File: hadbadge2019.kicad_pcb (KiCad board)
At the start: 4 copper layers, 88 x 140.5 mm, 194 parts, among them J1 Conn_02x05_Odd_Even, J10 Conn_01x02_Male, J11 NO STUFF, J12 NO STUFF, J2 USB_B_Micro, J3 NO STUFF, J4 HDMI_A_1.4, J5 FH26W-45S-0.3SHW(60), J6 Conn_02x20_Odd_Even, J7 Conn_02x03_Odd_Even, J8 Conn_02x03_Odd_Even, J9 Conn_01x02_Male, Q1 AO3400, Q2 AO3401, Q3 AO3400, Q4 AO3400, Q5 AO3400, SW1 Up, SW2 Down, SW3 Left, SW4 Right, SW5 A, SW6 B, SW7 Select, SW8 Start, SW9 SW_SPDT_shielded, U1 LFE5Ux-45F, U10 NS8002, U11 74LVC1G175, U12 RPM973, U2 LY68L6400SLIT, U3 LY68L6400SLIT, U4 W25Q128JVSIQ, U5 M3406, U6 XC6206P25, U7 XR1151, U8 74LVC1G3157, U9 XR1151, X1 X1G004481001400

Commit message: Starting to add fixes for final ver
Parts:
- added H1: MountingHole, MountingHole:MountingHole_3.5mm, B.Cu at (100.1, 111.4)
- added R72: 1K, Resistor_SMD:R_0603_1608Metric, B.Cu at (132.3, 141.5)
- R57: value 100 -> 1K
- moved R7 24.2 mm to (97.3, 101.5), turned to 270 degrees
- moved U8 7.42 mm to (100.1, 105.1)
- moved R56 3.78 mm to (105.2, 106.2), turned to 270 degrees
- moved C12 1.02 mm to (96.9, 126.2), turned to 0 degrees
- turned R69 to 0 degrees
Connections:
- D10 pad 2: CATR -> CATC
- D10 pad 3: CATG -> CATB
- D10 pad 4: CATB -> CATA
- D11 pad 2: CATR -> CATC
- D11 pad 3: CATG -> CATB
- D11 pad 4: CATB -> CATA
- D12 pad 2: CATR -> CATB
- D12 pad 3: CATG -> CATA
- D12 pad 4: CATB -> CATC
- D13 pad 2: CATR -> CATB
- D13 pad 3: CATG -> CATA
- D13 pad 4: CATB -> CATC
- D14 pad 2: CATR -> CATA
- D14 pad 3: CATG -> CATB
- D14 pad 4: CATB -> CATC
- D15 pad 2: CATR -> CATA
- D15 pad 3: CATG -> CATB
- D15 pad 4: CATB -> CATC
- D5 pad 2: CATR -> CATA
- D5 pad 3: CATG -> CATB
- D5 pad 4: CATB -> CATC
- D6 pad 2: CATR -> CATC
- D6 pad 3: CATG -> CATB
- D6 pad 4: CATB -> CATA
- D7 pad 2: CATR -> CATA
- D7 pad 3: CATG -> CATB
- D7 pad 4: CATB -> CATC
- D8 pad 2: CATR -> CATC
- D8 pad 3: CATG -> CATB
- D8 pad 4: CATB -> CATA
- D9 pad 2: CATR -> CATA
- D9 pad 3: CATG -> CATB
- D9 pad 4: CATB -> CATC
- J1 pad 4: (no net) -> Net-(J1-Pad4)
- Q3 pad 3: CATR -> CATA
- Q4 pad 3: CATG -> CATB
- Q5 pad 3: CATB -> CATC
- R69 pad 1: LEDR -> VIO
- R69 pad 2: GND -> LEDR
- SW9 pad 3: (no net) -> Net-(SW9-Pad3)
- U1 pad C13: (no net) -> Net-(U1-PadC13)
- U1 pad D12: (no net) -> Net-(U1-PadD12)
- U1 pad D13: (no net) -> Net-(U1-PadD13)
- U1 pad D14: (no net) -> Net-(U1-PadD14)
- U1 pad D15: (no net) -> Net-(U1-PadD15)
- U1 pad D7: (no net) -> Net-(U1-PadD7)
- U1 pad D8: (no net) -> Net-(U1-PadD8)
- U1 pad E10: (no net) -> Net-(U1-PadE10)
- U1 pad E11: (no net) -> Net-(U1-PadE11)
- U1 pad E12: (no net) -> Net-(U1-PadE12)
- U1 pad E13: (no net) -> Net-(U1-PadE13)
- U1 pad E14: (no net) -> Net-(U1-PadE14)
- U1 pad E15: (no net) -> Net-(U1-PadE15)
- U1 pad E16: (no net) -> GENIO_29
- U1 pad E18: (no net) -> Net-(U1-PadE18)
- U1 pad E6: (no net) -> Net-(U1-PadE6)
- U1 pad E7: (no net) -> Net-(U1-PadE7)
- U1 pad E8: (no net) -> Net-(U1-PadE8)
- U1 pad E9: (no net) -> Net-(U1-PadE9)
- U1 pad F16: (no net) -> Net-(U1-PadF16)
- U1 pad F18: (no net) -> GENIO_25
- U1 pad F5: (no net) -> Net-(U1-PadF5)
- U1 pad G16: (no net) -> Net-(U1-PadG16)
- U1 pad G5: (no net) -> Net-(U1-PadG5)
- U1 pad H16: (no net) -> GENIO_26
- U1 pad H3: (no net) -> Net-(U1-PadH3)
- U1 pad H4: (no net) -> Net-(U1-PadH4)
- U1 pad H5: (no net) -> Net-(U1-PadH5)
- U1 pad J17: (no net) -> Net-(U1-PadJ17)
- U1 pad J18: (no net) -> Net-(U1-PadJ18)
- U1 pad J5: (no net) -> Net-(U1-PadJ5)
- U1 pad K16: (no net) -> Net-(U1-PadK16)
- U1 pad K17: (no net) -> Net-(U1-PadK17)
- U1 pad K5: (no net) -> Net-(U1-PadK5)
- U1 pad L19: (no net) -> Net-(U1-PadL19)
- U1 pad L5: (no net) -> Net-(U1-PadL5)
- U1 pad M17: (no net) -> Net-(U1-PadM17)
- U1 pad M18: (no net) -> Net-(U1-PadM18)
- U1 pad M19: (no net) -> Net-(U1-PadM19)
- U1 pad M5: (no net) -> Net-(U1-PadM5)
- U1 pad N16: (no net) -> Net-(U1-PadN16)
- U1 pad N17: (no net) -> Net-(U1-PadN17)
- U1 pad N18: (no net) -> Net-(U1-PadN18)
- U1 pad N5: (no net) -> Net-(U1-PadN5)
- U1 pad P16: (no net) -> Net-(U1-PadP16)
- U1 pad P17: (no net) -> Net-(U1-PadP17)
- U1 pad P18: (no net) -> Net-(U1-PadP18)
- U1 pad R17: (no net) -> Net-(U1-PadR17)
- U1 pad R3: (no net) -> Net-(U1-PadR3)
- U1 pad T17: (no net) -> Net-(U1-PadT17)
- U1 pad T2: (no net) -> Net-(U1-PadT2)
- U1 pad T20: (no net) -> Net-(U1-PadT20)
- U1 pad T3: (no net) -> Net-(U1-PadT3)
- U1 pad V1: (no net) -> Net-(U1-PadV1)
- U1 pad W10: (no net) -> Net-(U1-PadW10)
- U1 pad W11: (no net) -> Net-(U1-PadW11)
- U1 pad W13: (no net) -> Net-(U1-PadW13)
- U1 pad W14: (no net) -> Net-(U1-PadW14)
- U1 pad W17: (no net) -> Net-(U1-PadW17)
- U1 pad W18: (no net) -> Net-(U1-PadW18)
- U1 pad W20: (no net) -> Net-(U1-PadW20)
- U1 pad W4: (no net) -> Net-(U1-PadW4)
- U1 pad W5: (no net) -> Net-(U1-PadW5)
- U1 pad W8: (no net) -> Net-(U1-PadW8)
- U1 pad W9: (no net) -> Net-(U1-PadW9)
- U1 pad Y11: (no net) -> Net-(U1-PadY11)
- U1 pad Y12: (no net) -> Net-(U1-PadY12)
- U1 pad Y14: (no net) -> Net-(U1-PadY14)
- U1 pad Y15: (no net) -> Net-(U1-PadY15)
- U1 pad Y16: (no net) -> Net-(U1-PadY16)
- U1 pad Y17: (no net) -> Net-(U1-PadY17)
- U1 pad Y19: (no net) -> Net-(U1-PadY19)
- U1 pad Y5: (no net) -> Net-(U1-PadY5)
- U1 pad Y6: (no net) -> Net-(U1-PadY6)
- U1 pad Y7: (no net) -> Net-(U1-PadY7)
- U1 pad Y8: (no net) -> Net-(U1-PadY8)
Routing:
- net CATA: track 0.00 -> 191.5 mm, vias 0 -> 12
- net CATC: track 0.00 -> 186.8 mm, vias 0 -> 6
- net CATR: track 182.4 -> 0.00 mm, vias 6 -> 0
- net CATG: track 180.4 -> 0.00 mm, vias 16 -> 0
- net VIO: track 95.7 -> 106.2 mm, vias 21 -> 23
- net Net-(U11-Pad4): track 7.86 -> 15.8 mm
- net CATB: track 191.9 -> 185.6 mm, vias 4 -> 15
- net LED11: track 19.0 -> 24.6 mm, vias 1 -> 2
- net BTN_UP: track 33.9 -> 39.1 mm
- net GND: track 327.9 -> 322.8 mm
- net /FPGA/FLASH_CS_INT: track 42.1 -> 37.2 mm, vias 4 -> 3
- net ADCREF: track 24.7 -> 26.1 mm
- net LED6: track 97.6 -> 99.0 mm
- net LED4: track 99.8 -> 101.2 mm
- net LED5: track 98.5 -> 99.8 mm
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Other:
- board text added: "2019, SPRITE_TM SPRITESMODS.COM"
- board text added: "GPIO3 DRM"
- board text added: "Hackaday Supercon 2019 Badge Final Version All the bugs on this badge not caught in the prototypes are now official features."
- board text added: "J11: PMOD PMODB4 PMODA4 PMODB3 PMODA3 PMODB2 PMODA2 PMODB1 PMODA1 GND GND 3V3 3V3"
- board text added: "J1: RX TX TCK TMS TDO TDI KEY 3V3 GND VBAT"
- board text added: "J3 (OTHER SIDE): INSERT SPEAKER HERE."
- board text added: "J8 & J11: SAO V1.69 BIS X-TREME! HDRS"
- board text added: "VIO GND SCL SDA GPIO2 GPIO1"
- board text removed: "DRM GPIO3"
- board text removed: "Hackaday Supercon 2019 Badge Proto v3 If you have this, you are hyper-l33t, and/or get to suffer through the last few bugs that the final version won't have."
- board text removed: "J11: PMOD 3V3 3V3 GND GND PMODA1 PMODB1 PMODA2 PMODB2 PMODA3 PMODB3 PMODA4 PMODB4"
- board text removed: "J1: VBAT GND 3V3 KEY TDI TDO TMS TCK TX RX"
- board text removed: "J8-J11: SAO V1.69 BIS X-TREME! HDRS GPIO1 GPIO2 SDA SCL GND 3V3"

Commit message: Final version
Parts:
- added REF**: mouse_bite_6, lib:mouse_bite_6, F.Cu at (143.3, 25.2)
- added REF**: mouse_bite_6, lib:mouse_bite_6, F.Cu at (113.7, 25.2)
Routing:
- net VBAT: track 306.6 -> 302.4 mm
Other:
- outline, holes or cut-outs redrawn
- board text added: "BAT NEG"
- board text added: "BAT POS"
- board text added: "REMOVE ME"

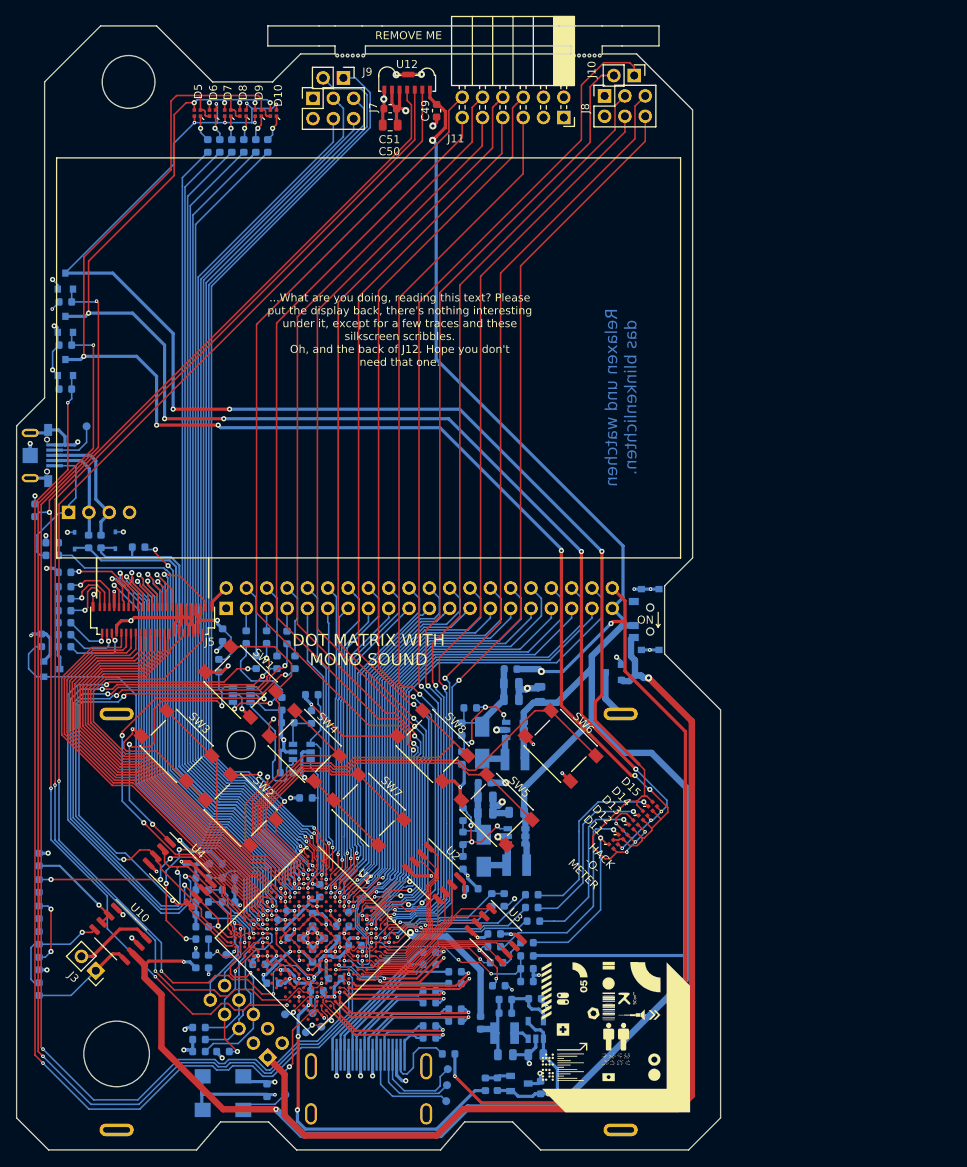
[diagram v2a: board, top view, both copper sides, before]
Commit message: Final changes: add some fiducials, clean up vias. Ready for prod, I hope.
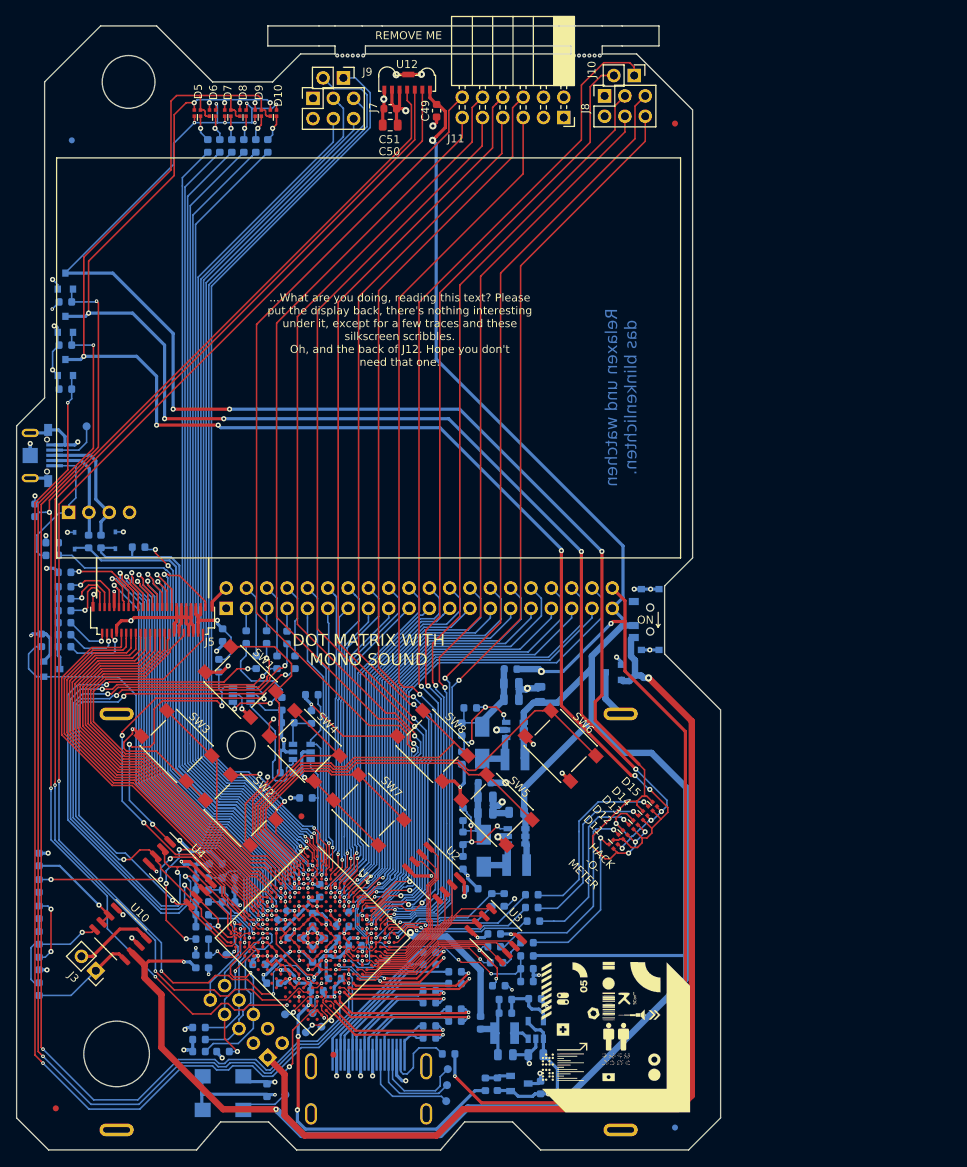
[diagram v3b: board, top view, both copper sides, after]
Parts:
- added FID1: Fiducial, Fiducial:Fiducial_0.75mm_Mask1.5mm, F.Cu at (107.6, 120.3)
- added FID2: Fiducial, Fiducial:Fiducial_0.75mm_Mask1.5mm, F.Cu at (111.6, 150.1)
- added FID3: Fiducial, Fiducial:Fiducial_0.75mm_Mask1.5mm, F.Cu at (76.9, 156.8)
- added FID4: Fiducial, Fiducial:Fiducial_0.75mm_Mask1.5mm, F.Cu at (154.3, 33.7)
- added FID5: Fiducial, Fiducial:Fiducial_0.75mm_Mask1.5mm, B.Cu at (154.3, 159.2)
- added FID6: Fiducial, Fiducial:Fiducial_0.75mm_Mask1.5mm, B.Cu at (78.9, 35.8)
- SW1: value Up -> Up (RED)
- SW2: value Down -> Down (RED)
- SW3: value Left -> Left (RED)
- SW4: value Right -> Right (RED)
- SW5: value A -> A (RED)
- SW6: value B -> B (RED)
- SW7: value Select -> Select (BLUE)
- SW8: value Start -> Start (BLUE)
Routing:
- net CATC: track 186.8 -> 187.3 mm

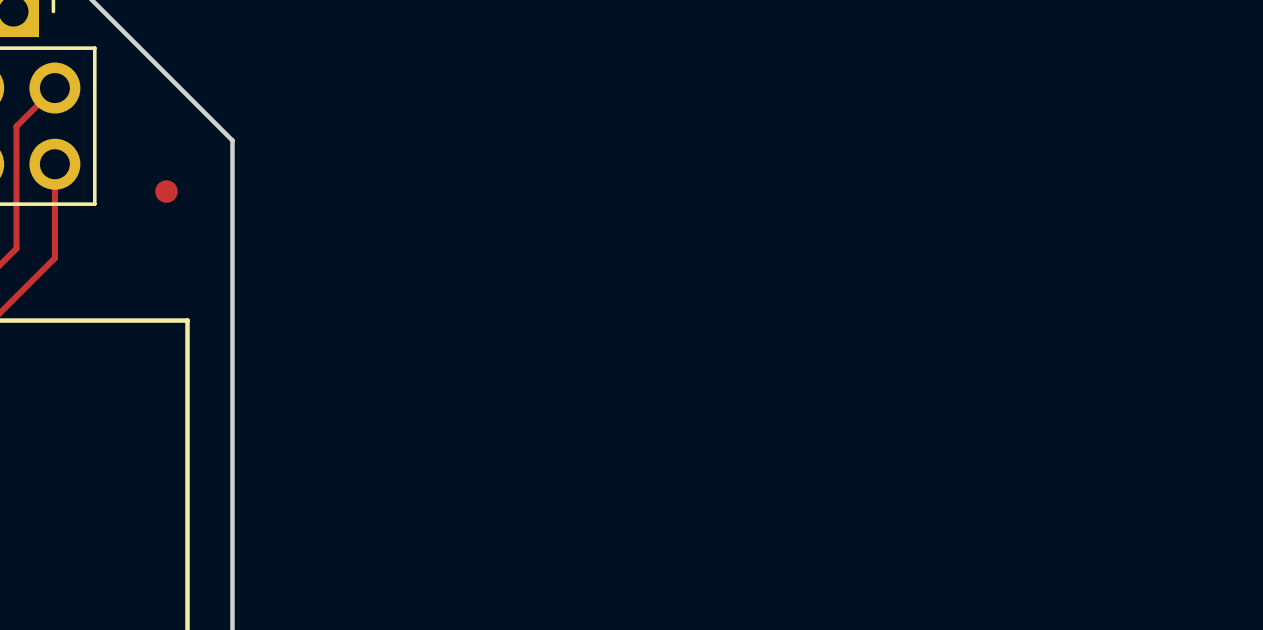
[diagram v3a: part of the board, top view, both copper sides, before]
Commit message: Add known issues
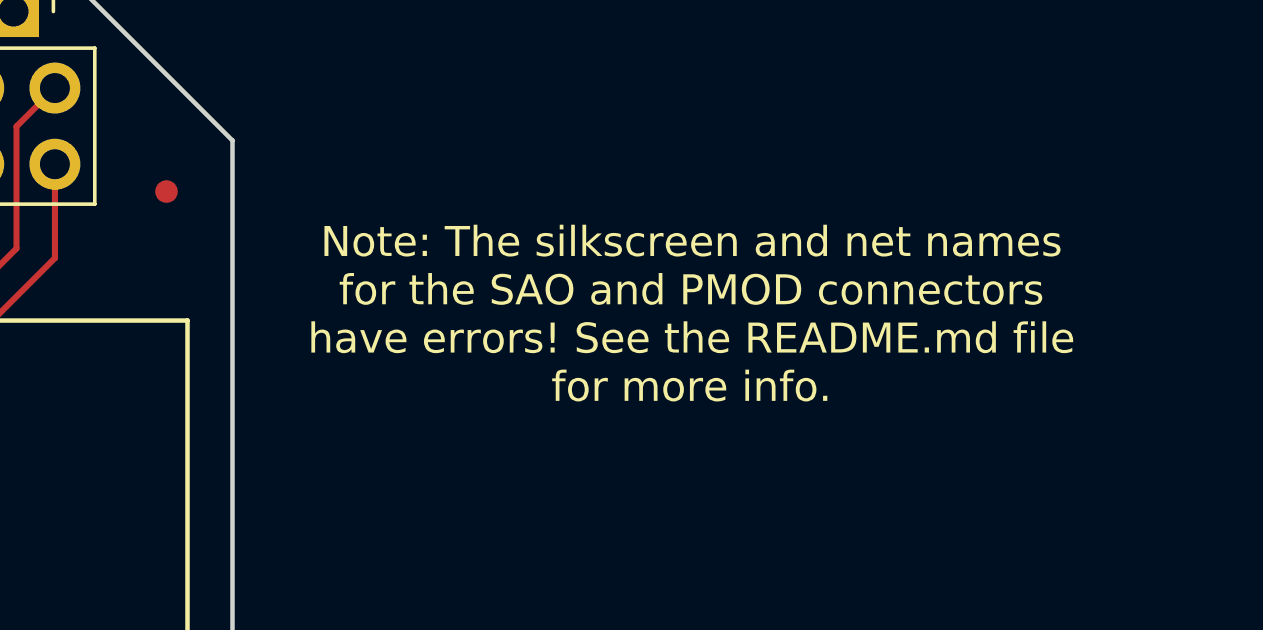
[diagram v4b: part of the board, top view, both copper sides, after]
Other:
- board text added: "Note: The silkscreen and net names for the SAO and PMOD connectors have errors! See the README.md file for more info."
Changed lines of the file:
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@@
-(kicad_pcb (version 20171130) (host pcbnew 5.1.4+dfsg1-1)
+(kicad_pcb (version 20171130) (host pcbnew 5.1.4+dfsg1-2)
   (general
     (thickness 1.6)
-    (drawings 93)
+    (drawings 94)
     (tracks 4139)
     (zones 0)
@@
     (34 B.Paste user hide)
     (35 F.Paste user hide)
-    (36 B.SilkS user hide)
+    (36 B.SilkS user)
     (37 F.SilkS user)
     (38 B.Mask user hide)
@@
     )
   )
+  (gr_text "Note: The silkscreen and net names\nfor the SAO and PMOD connectors\nhave errors! See the README.md file\nfor more info." (at 171.8 37.8) (layer F.SilkS)
+    (effects (font (size 1 1) (thickness 0.15)))
+  )
   (gr_text "BAT POS" (at 158.1 110.6 90) (layer B.SilkS)
